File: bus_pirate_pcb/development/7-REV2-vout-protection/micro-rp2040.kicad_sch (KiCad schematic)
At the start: 62 parts, among them J201 Conn_01x03, J202 TYPE-C-31-M-12, Q1 2N7002KT, Q5 2N7002KT, SW101 TS3425BA 098 2.5H 250gf, SW102 TS3315A 250gf 025, U1 RP2350B, U102 W25Q128JVSIQ, U105 MT29F2G01ABAGDWB-IT:G, U16 SP3002-04JTG, U17 TLV75801PDRV, U401 ME6211A33PG-N, U8 APS6404L-3SQR-ZR, Y101 ABM8-272-T3

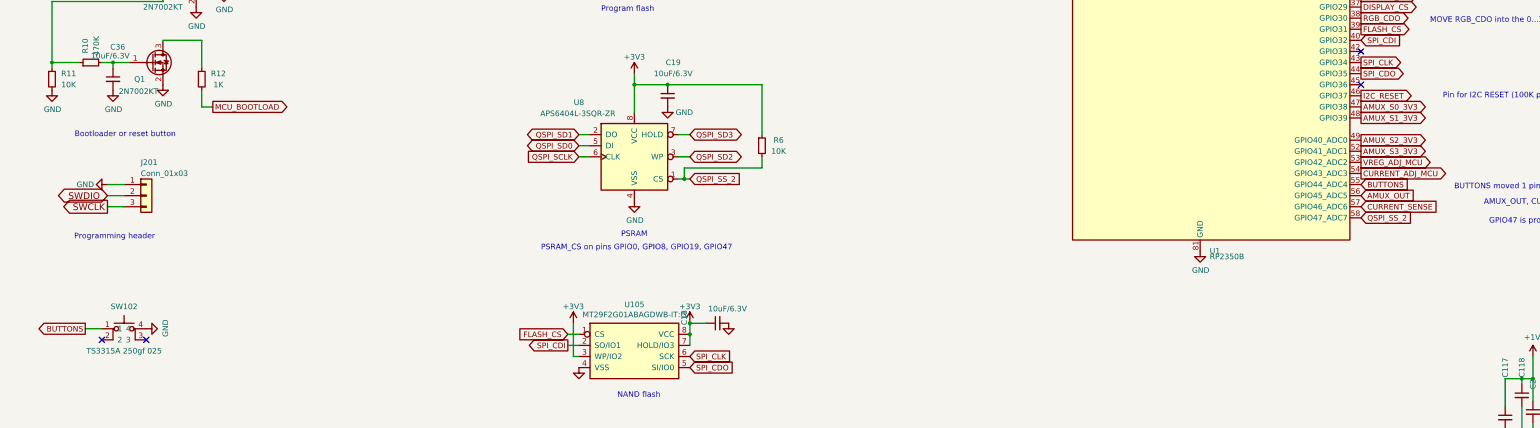
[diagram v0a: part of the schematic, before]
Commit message: 7R2 with vout protection
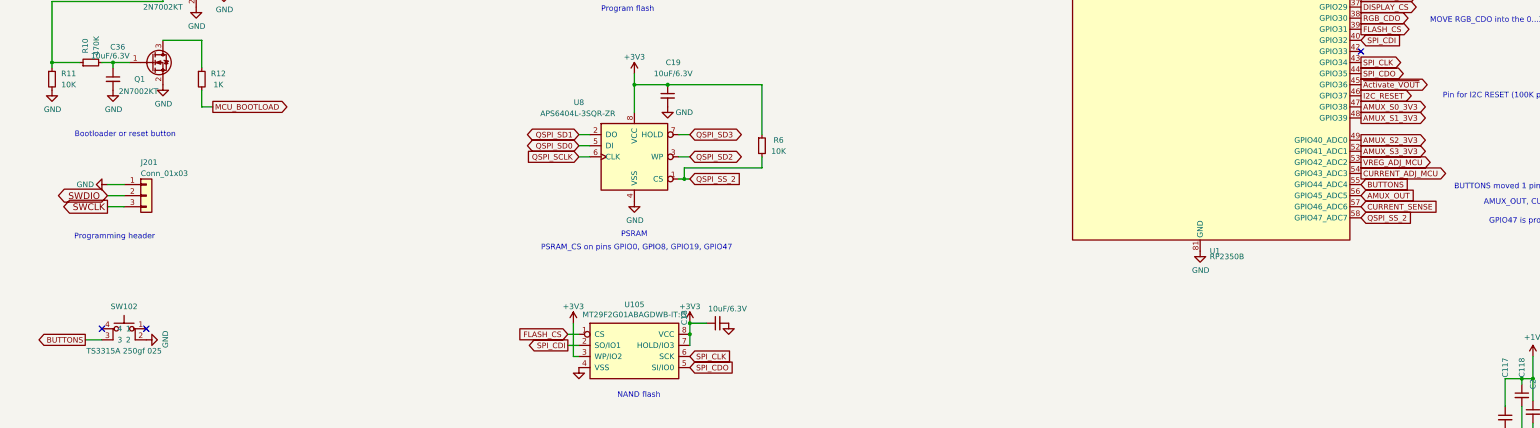
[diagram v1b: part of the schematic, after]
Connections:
- net BUTTONS: now also SW102.3; no longer SW102.1
- net GND: now also SW102.2; no longer SW102.4
- net ~{Activate_VOUT}: now reaches U1.45 (GPIO36)
- no-connect marks 12 -> 11
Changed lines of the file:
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@@
 	)
 	(no_connect
-		(at 328.93 157.48)
-	)
-	(no_connect
 		(at 328.93 109.22)
 	)
@@
 	)
 	(no_connect
-		(at 40.64 215.9)
+		(at 40.64 213.36)
 	)
 	(no_connect
-		(at 50.8 215.9)
+		(at 50.8 213.36)
 	)
 	(no_connect
@@
 	(wire
 		(pts
-			(xy 36.83 213.36) (xy 40.64 213.36)
+			(xy 36.83 215.9) (xy 40.64 215.9)
 		)
 		(stroke
@@
 		)
 	)
+	(global_label "~{Activate_VOUT}"
+		(shape output)
+		(at 328.93 157.48 0)
+		(fields_autoplaced yes)
+		(effects
+			(font
+				(size 1.27 1.27)
+			)
+			(justify left)
+		)
+		(property "Intersheetrefs" "${INTERSHEET_REFS}"
+			(at 344.3844 157.48 0)
+			(effects
+				(font
+					(size 1.27 1.27)
+				)
+				(justify left)
+				(hide yes)
+			)
+		)
+	)
 	(global_label "LA_BPIO3_TVS"
 		(shape input)
@@
 	(global_label "BUTTONS"
 		(shape output)
-		(at 36.83 213.36 180)
+		(at 36.83 215.9 180)
 		(effects
 			(font
@@
 		)
 		(property "Intersheetrefs" "${INTERSHEET_REFS}"
-			(at 36.83 213.36 0)
+			(at 36.83 215.9 0)
 			(effects
 				(font
@@
 		(lib_id "dp-switch:4P_button_sw")
 		(at 45.72 214.63 0)
+		(mirror y)
 		(unit 1)
 		(exclude_from_sim no)
@@
 	(symbol
 		(lib_id "power:GND")
-		(at 50.8 213.36 90)
+		(at 50.8 215.9 90)
 		(unit 1)
 		(exclude_from_sim no)
@@
 		(on_board yes)
 		(dnp no)
+		(fields_autoplaced yes)
 		(property "Reference" "#PWR028"
-			(at 57.15 213.36 0)
+			(at 57.15 215.9 0)
 			(effects
 				(font
@@
 		)
 		(property "Value" "GND"
-			(at 55.1942 213.233 0)
+			(at 55.1942 215.773 0)
 			(effects
 				(font
@@
 		)
 		(property "Footprint" ""
-			(at 50.8 213.36 0)
+			(at 50.8 215.9 0)
 			(effects
 				(font
@@
 		)
 		(property "Datasheet" ""
-			(at 50.8 213.36 0)
+			(at 50.8 215.9 0)
 			(effects
 				(font
@@
 		)
 		(property "Description" ""
-			(at 50.8 213.36 0)
+			(at 50.8 215.9 0)
 			(effects
 				(font
